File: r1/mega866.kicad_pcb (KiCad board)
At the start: 2 copper layers, 2 parts, among them J1 5650908-5, J2 5650908-5

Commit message: cleaner drc / fix errors
Signed-off-by: John McMaster <johndmcmaster@gmail.com>
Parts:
- added D1: LED, LED_SMD:LED_0603_1608Metric, F.Cu at (-44.7, 45.7)
- added D2: LED, LED_SMD:LED_0603_1608Metric, F.Cu at (-48.8, 45.7)
- added J5: Conn_01x02_Male, Connector_PinHeader_2.54mm:PinHeader_1x02_P2.54mm_Vertical, F.Cu at (-91.9, 100.4)
- added J8: Conn_01x02_Male, Connector_PinHeader_2.54mm:PinHeader_1x02_P2.54mm_Vertical, F.Cu at (-67.8, 46.8)
- added Q1: BSS84, Package_TO_SOT_SMD:SOT-23, F.Cu at (-63.0, 46.6)
- added Q2: 2N7002, Package_TO_SOT_SMD:SOT-23, F.Cu at (-53.2, 46.6)
- added Q3: 2N7002, Package_TO_SOT_SMD:SOT-23, F.Cu at (-58.1, 46.6)
- added R1: R, Resistor_SMD:R_0603_1608Metric, F.Cu at (-47.4, 48.3)
- added R10: NOLOAD, Resistor_SMD:R_0603_1608Metric, F.Cu at (-43.4, 53.2)
- added R11: 4.7k, Resistor_SMD:R_0603_1608Metric, F.Cu at (-51.4, 50.1)
- added R12: 0, Resistor_SMD:R_0603_1608Metric, F.Cu at (-60.1, 53.2)
- added R13: 0, Resistor_SMD:R_0603_1608Metric, F.Cu at (-68.1, 55.7)
- added R14: 0, Resistor_SMD:R_0603_1608Metric, F.Cu at (-39.4, 50.7)
- added R15: 100k, Resistor_SMD:R_0603_1608Metric, F.Cu at (-64.1, 53.2)
- added R17: 4.7K, Resistor_SMD:R_0603_1608Metric, F.Cu at (-59.5, 50.1)
- added R18: 0, Resistor_SMD:R_0603_1608Metric, F.Cu at (-56.1, 55.1)
- added R19: 0, Resistor_SMD:R_0603_1608Metric, F.Cu at (-52.1, 52.6)
- added R2: R, Resistor_SMD:R_0603_1608Metric, F.Cu at (-47.4, 50.8)
- added R20: 0, Resistor_SMD:R_0603_1608Metric, F.Cu at (-52.1, 55.1)
- added R21: 0, Resistor_SMD:R_0603_1608Metric, F.Cu at (-36.7, 48.2)
- added R22: 0, Resistor_SMD:R_0603_1608Metric, F.Cu at (-40.7, 45.7)
- added R23: 0, Resistor_SMD:R_0603_1608Metric, F.Cu at (-55.4, 50.1)
- added R3: 47k, Resistor_SMD:R_0603_1608Metric, F.Cu at (-63.5, 50.7)
- added R4: 4.7k, Resistor_SMD:R_0603_1608Metric, F.Cu at (-36.7, 45.7)
- added R5: 4.7k, Resistor_SMD:R_0603_1608Metric, F.Cu at (-32.7, 45.7)
- added R6: 47k, Resistor_SMD:R_0603_1608Metric, F.Cu at (-39.4, 53.2)
- added R7: NOLOAD, Resistor_SMD:R_0603_1608Metric, F.Cu at (-40.7, 48.2)
- added R8: NOLOAD, Resistor_SMD:R_0603_1608Metric, F.Cu at (-56.1, 52.6)
- added R9: NOLOAD, Resistor_SMD:R_0603_1608Metric, F.Cu at (-43.4, 50.7)
- added U1: Pico, mega866:RPi_Pico_SMD_TH, F.Cu at (-82.2, 71.0)

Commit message: WIP
Signed-off-by: John McMaster <johndmcmaster@gmail.com>
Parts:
- added J10: Conn_01x06_Male, Connector_PinHeader_2.54mm:PinHeader_1x06_P2.54mm_Vertical, B.Cu at (171.4, 149.7)
- added J3: tl866_dip40, mega866:tl866, F.Cu at (64.6, 4.91)
- added J4: Conn_01x06_Male, Connector_PinHeader_2.54mm:PinHeader_1x06_P2.54mm_Vertical, B.Cu at (116.8, 30.3)
- added J5: tl866_dip40, mega866:tl866, F.Cu at (211.9, 53.2)
- added J6: Conn_01x06_Male, Connector_PinHeader_2.54mm:PinHeader_1x06_P2.54mm_Vertical, B.Cu at (171.4, 78.6)
- added J7: tl866_dip40, mega866:tl866, F.Cu at (64.6, 126.8)
- added J8: Conn_01x06_Male, Connector_PinHeader_2.54mm:PinHeader_1x06_P2.54mm_Vertical, B.Cu at (116.8, 101.4)
- added J9: tl866_dip40, mega866:tl866, F.Cu at (211.9, 175.1)
- D1, D2, Q1, Q2, Q3, R1, R10, R11, R12, R13, R14, R15, R17, R18, R19, R2, R20, R21, R22, R23, R3, R4, R5, R6, R7, R8, R9, U1: moved to B.Cu
- J1: renamed from J2; value 5650908-5 -> ZSM1-SM1; footprint 5650908-5:TE_5650908-5 -> mega866:5650470-5
- J11: renamed from J5; moved to B.Cu
- J12: renamed from J8; moved to B.Cu
- J2: renamed from J1; value 5650908-5 -> ZSM1-SM2; footprint 5650908-5:TE_5650908-5 -> mega866:5650470-5
- moved R15 235.8 mm to (151.1, -43.2), turned to 180 degrees
- moved R12 228.5 mm to (147.1, -43.2), turned to 180 degrees
- moved R17 227.4 mm to (146.5, -46.3), turned to 180 degrees
- moved R2 221.9 mm to (137.2, 174.0), turned to 180 degrees
- moved D2 221.7 mm to (132.1, 174.0), turned to 180 degrees
- moved U1 220.3 mm to (137.3, 90.2)
- moved R11 213.0 mm to (138.5, -46.3), turned to 180 degrees
- moved R13 209.2 mm to (129.5, -12.7), turned to 180 degrees
- moved D1 207.9 mm to (118.9, 174.0), turned to 180 degrees
- moved J11 207.3 mm to (114.3, 121.9)
- moved R1 204.8 mm to (114.3, 174.0), turned to 180 degrees
- moved J12 201.2 mm to (133.3, 50.8), turned to -90 degrees
- moved Q3 200.7 mm to (125.7, 127.0)
- moved R3 196.7 mm to (119.4, 123.2), turned to 90 degrees
- moved Q1 194.6 mm to (113.0, 129.5), turned to 180 degrees
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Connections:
- J1 pad A1: (no net) -> GND
- J1 pad A10: (no net) -> G037
- J1 pad A11: (no net) -> G035
- J1 pad A12: (no net) -> G033
- J1 pad A13: (no net) -> G031
- J1 pad A14: (no net) -> G029
- J1 pad A15: (no net) -> G027
- J1 pad A16: (no net) -> G025
- J1 pad A17: (no net) -> G023
- J1 pad A18: (no net) -> G021
- J1 pad A19: (no net) -> G019
- J1 pad A2: (no net) -> Net-(J1-PadA2)
- J1 pad A20: (no net) -> G017
- J1 pad A21: (no net) -> G015
- J1 pad A22: (no net) -> G013
- J1 pad A23: (no net) -> G011
- J1 pad A24: (no net) -> G009
- J1 pad A25: (no net) -> G007
- J1 pad A26: (no net) -> G005
- J1 pad A27: (no net) -> G003
- J1 pad A28: (no net) -> G001
- J1 pad A29: (no net) -> GND
- J1 pad A3: (no net) -> Net-(J1-PadA2)
- J1 pad A30: (no net) -> P2R
- J1 pad A31: (no net) -> VCC
- J1 pad A32: (no net) -> GND
- J1 pad A4: (no net) -> GND
- J1 pad A5: (no net) -> G047
- J1 pad A6: (no net) -> G045
- J1 pad A7: (no net) -> G043
- J1 pad A8: (no net) -> G041
- J1 pad A9: (no net) -> G039
- J1 pad B1: (no net) -> G159
- J1 pad B10: (no net) -> G141
- J1 pad B11: (no net) -> G139
- J1 pad B12: (no net) -> G137
- J1 pad B13: (no net) -> G135
- J1 pad B14: (no net) -> G133
- J1 pad B15: (no net) -> G131
- J1 pad B16: (no net) -> G129
- J1 pad B17: (no net) -> G127
- J1 pad B18: (no net) -> G125
- J1 pad B19: (no net) -> G123
- J1 pad B2: (no net) -> G157
- J1 pad B20: (no net) -> G121
- J1 pad B21: (no net) -> G119
- J1 pad B22: (no net) -> G117
- J1 pad B23: (no net) -> G115
- J1 pad B24: (no net) -> G113
- J1 pad B25: (no net) -> G111
- J1 pad B26: (no net) -> G109
- J1 pad B27: (no net) -> G107
- J1 pad B28: (no net) -> G105
- J1 pad B29: (no net) -> G103
- J1 pad B3: (no net) -> G155
- J1 pad B30: (no net) -> G101
- J1 pad B31: (no net) -> G099
- J1 pad B32: (no net) -> G097
- J1 pad B4: (no net) -> G153
- J1 pad B5: (no net) -> G151
- J1 pad B6: (no net) -> G149
- J1 pad B7: (no net) -> G147
- J1 pad B8: (no net) -> G145
- J1 pad B9: (no net) -> G143
- J1 pad C1: (no net) -> BPM_SR_CLK
- J1 pad C10: (no net) -> G087
- J1 pad C11: (no net) -> GND
- J1 pad C12: (no net) -> G085
- J1 pad C13: (no net) -> G083
- J1 pad C14: (no net) -> G081
- J1 pad C15: (no net) -> G079
- J1 pad C16: (no net) -> G077
- J1 pad C17: (no net) -> GND
- J1 pad C18: (no net) -> G075
- J1 pad C19: (no net) -> G073
- J1 pad C2: (no net) -> BPM_SR_D
- J1 pad C20: (no net) -> G071
- J1 pad C21: (no net) -> G069
- J1 pad C22: (no net) -> G067
- J1 pad C23: (no net) -> GND
- J1 pad C24: (no net) -> G065
- J1 pad C25: (no net) -> G063
- J1 pad C26: (no net) -> G061
- J1 pad C27: (no net) -> G059
- J1 pad C28: (no net) -> G057
- J1 pad C29: (no net) -> G055
- J1 pad C3: (no net) -> Net-(J1-PadC3)
- J1 pad C30: (no net) -> G053
- J1 pad C31: (no net) -> G051
- J1 pad C32: (no net) -> G049
- J1 pad C4: (no net) -> Net-(J1-PadC4)
- J1 pad C5: (no net) -> SM1_C5
- J1 pad C6: (no net) -> G095
- J1 pad C7: (no net) -> G093
- J1 pad C8: (no net) -> G091
- J1 pad C9: (no net) -> G089
- J11 pad 1: P2R -> Net-(J11-Pad1)
- J11 pad 2: COIL_GPIO -> VCC
- J12 pad 1: Net-(J8-Pad1) -> P2R
- J12 pad 2: VCC -> COIL_GPIO
- J2 pad A1: (no net) -> EEPROM_DO
- J2 pad A10: (no net) -> G088
- J2 pad A11: (no net) -> GND
- J2 pad A12: (no net) -> G086
- J2 pad A13: (no net) -> G084
- J2 pad A14: (no net) -> G082
- J2 pad A15: (no net) -> G080
- J2 pad A16: (no net) -> G078
- J2 pad A17: (no net) -> GND
- J2 pad A18: (no net) -> G076
- J2 pad A19: (no net) -> G074
- J2 pad A2: (no net) -> EEPROM_DI
- J2 pad A20: (no net) -> G072
- J2 pad A21: (no net) -> G070
- J2 pad A22: (no net) -> G068
- J2 pad A23: (no net) -> GND
- J2 pad A24: (no net) -> G066
- J2 pad A25: (no net) -> G064
- J2 pad A26: (no net) -> G062
- J2 pad A27: (no net) -> G060
- J2 pad A28: (no net) -> G058
- J2 pad A29: (no net) -> G056
- J2 pad A3: (no net) -> EEPROM_CLK
- J2 pad A30: (no net) -> G054
- J2 pad A31: (no net) -> G052
- J2 pad A32: (no net) -> G050
- J2 pad A4: (no net) -> EEPROM_CS
- J2 pad A5: (no net) -> SM2_A5
- J2 pad A6: (no net) -> G096
- J2 pad A7: (no net) -> G094
- J2 pad A8: (no net) -> G092
- J2 pad A9: (no net) -> G090
- J2 pad B1: (no net) -> G160
- J2 pad B10: (no net) -> G142
- J2 pad B11: (no net) -> G140
- J2 pad B12: (no net) -> G138
- J2 pad B13: (no net) -> G136
- J2 pad B14: (no net) -> G134
- J2 pad B15: (no net) -> G132
- J2 pad B16: (no net) -> G130
- J2 pad B17: (no net) -> G128
- J2 pad B18: (no net) -> G126
- J2 pad B19: (no net) -> G124
- J2 pad B2: (no net) -> G158
- J2 pad B20: (no net) -> G122
- J2 pad B21: (no net) -> G120
- J2 pad B22: (no net) -> G118
- J2 pad B23: (no net) -> G116
- J2 pad B24: (no net) -> G114
- J2 pad B25: (no net) -> G112
- J2 pad B26: (no net) -> G110
- J2 pad B27: (no net) -> G108
- J2 pad B28: (no net) -> G106
- J2 pad B29: (no net) -> G104
- J2 pad B3: (no net) -> G156
- J2 pad B30: (no net) -> G102
- J2 pad B31: (no net) -> G100
- J2 pad B32: (no net) -> G098
- J2 pad B4: (no net) -> G154
- J2 pad B5: (no net) -> G152
- J2 pad B6: (no net) -> G150
- J2 pad B7: (no net) -> G148
- J2 pad B8: (no net) -> G146
- J2 pad B9: (no net) -> G144
- J2 pad C1: (no net) -> GND
- J2 pad C10: (no net) -> G038
- J2 pad C11: (no net) -> G036
- J2 pad C12: (no net) -> G034
- J2 pad C13: (no net) -> G032
- J2 pad C14: (no net) -> G030
- J2 pad C15: (no net) -> G028
- J2 pad C16: (no net) -> G026
- J2 pad C17: (no net) -> G024
- J2 pad C18: (no net) -> G022
- J2 pad C19: (no net) -> G020
- J2 pad C2: (no net) -> SM_DET
- J2 pad C20: (no net) -> G018
- J2 pad C21: (no net) -> G016
- J2 pad C22: (no net) -> G014
- J2 pad C23: (no net) -> G012
- J2 pad C24: (no net) -> G010
- J2 pad C25: (no net) -> G008
- J2 pad C26: (no net) -> G006
- J2 pad C27: (no net) -> G004
- J2 pad C28: (no net) -> G002
- J2 pad C29: (no net) -> GND
- J2 pad C3: (no net) -> SM2_C3
- J2 pad C30: (no net) -> Net-(J2-PadC30)
- J2 pad C31: (no net) -> unconnected-(J2-PadC31)
- J2 pad C32: (no net) -> GND
- J2 pad C4: (no net) -> COILP
- J2 pad C5: (no net) -> G048
- J2 pad C6: (no net) -> G046
- J2 pad C7: (no net) -> G044
- J2 pad C8: (no net) -> G042
- J2 pad C9: (no net) -> G040
- Q1 pad 1: Net-(J8-Pad1) -> Net-(Q1-Pad1)
- Q1 pad 2: Net-(J8-Pad1) -> Net-(J11-Pad1)
- Q1 pad 3: Net-(J8-Pad1) -> COILP
- Q2 pad 3: Net-(Q1-Pad4) -> Net-(Q1-Pad1)
- R11 pad 1: EEPROM CS -> EEPROM_CS
- R3 pad 1: Net-(Q1-Pad4) -> Net-(Q1-Pad1)
- R3 pad 2: Net-(J8-Pad1) -> Net-(J11-Pad1)
- U1 pad 1: EEPROM DO -> EEPROM_DO
- U1 pad 2: EEPROM CS -> EEPROM_CS
- U1 pad 4: EEPROM CLK -> EEPROM_CLK
- U1 pad 5: EEPROM DI -> EEPROM_DI
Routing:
- net G048: track 0.00 -> 103.5 mm
- net G044: track 0.00 -> 101.0 mm
- net G040: track 0.00 -> 98.4 mm
- net G036: track 0.00 -> 95.9 mm
- net G032: track 0.00 -> 93.4 mm
- net G046: track 0.00 -> 91.2 mm
- net G028: track 0.00 -> 90.8 mm
- net G042: track 0.00 -> 88.6 mm
- net G024: track 0.00 -> 88.3 mm
- net G038: track 0.00 -> 86.1 mm
- net G020: track 0.00 -> 85.6 mm
- net G034: track 0.00 -> 83.8 mm
- net G016: track 0.00 -> 83.2 mm
- net G030: track 0.00 -> 81.0 mm
- net G012: track 0.00 -> 80.5 mm
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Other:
- board outline added: 10 x 4 mm

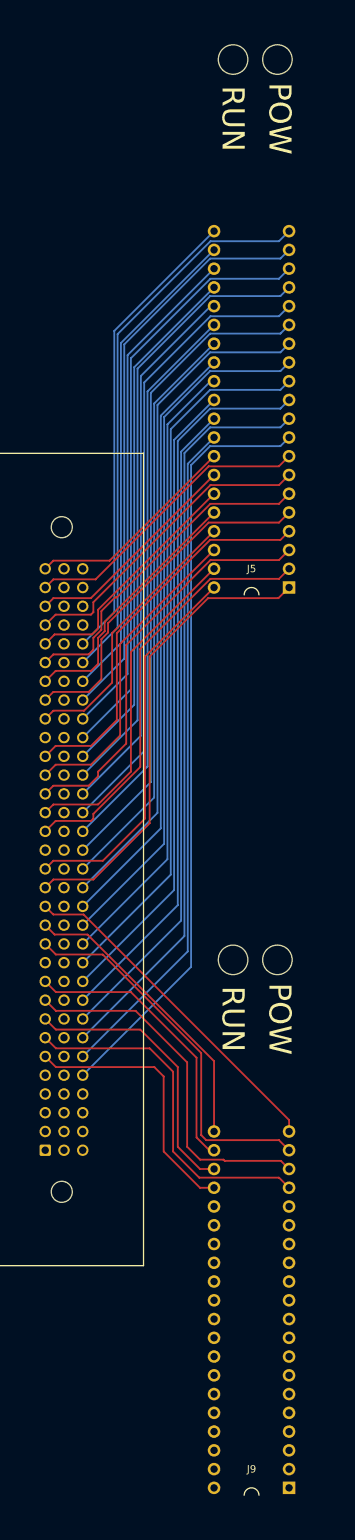
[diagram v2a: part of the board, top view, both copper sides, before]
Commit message: reassign pins for easier routing
Signed-off-by: John McMaster <johndmcmaster@gmail.com>
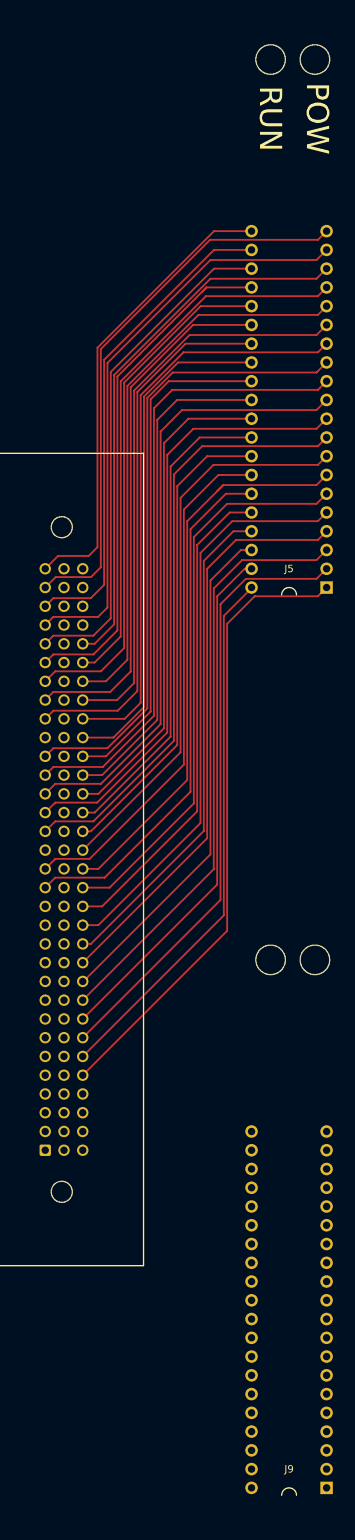
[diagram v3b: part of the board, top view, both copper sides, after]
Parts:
- moved J5 5.08 mm to (217.0, 53.2)
- moved J9 5.08 mm to (217.0, 175.1)
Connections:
- J5 pad 1: G080 -> G048
- J5 pad 10: G044 -> G074
- J5 pad 11: G040 -> G072
- J5 pad 12: G036 -> G070
- J5 pad 13: G032 -> G068
- J5 pad 14: G028 -> G010
- J5 pad 15: G024 -> G008
- J5 pad 16: G020 -> G006
- J5 pad 17: G016 -> G004
- J5 pad 18: G012 -> G002
- J5 pad 19: G008 -> G056
- J5 pad 2: G076 -> G044
- J5 pad 20: G004 -> G052
- J5 pad 21: G002 -> G050
- J5 pad 22: G006 -> G054
- J5 pad 23: G010 -> G058
- J5 pad 24: G014 -> G060
- J5 pad 25: G018 -> G062
- J5 pad 26: G022 -> G064
- J5 pad 27: G026 -> G066
- J5 pad 28: G030 -> G012
- J5 pad 29: G034 -> G014
- J5 pad 3: G072 -> G040
- J5 pad 30: G038 -> G016
- J5 pad 31: G042 -> G018
- J5 pad 32: G046 -> G020
- J5 pad 33: G050 -> G022
- J5 pad 34: G054 -> G078
- J5 pad 35: G058 -> G080
- J5 pad 36: G062 -> G030
- J5 pad 37: G066 -> G034
- J5 pad 38: G070 -> G038
- J5 pad 39: G074 -> G042
- J5 pad 4: G068 -> G036
- J5 pad 40: G078 -> G046
- J5 pad 5: G064 -> G032
- J5 pad 6: G060 -> G028
- J5 pad 7: G056 -> G026
- J5 pad 8: G052 -> G024
- J5 pad 9: G048 -> G076
- J9 pad 10: G122 -> G084
- J9 pad 11: G118 -> G082
- J9 pad 12: G114 -> G130
- J9 pad 13: G110 -> G126
- J9 pad 14: G106 -> G122
- J9 pad 15: G102 -> G118
- J9 pad 16: G098 -> G114
- J9 pad 17: G094 -> G110
- J9 pad 18: G090 -> G106
- J9 pad 19: G086 -> G102
- J9 pad 20: G082 -> G098
- J9 pad 21: G084 -> G100
- J9 pad 22: G088 -> G104
- J9 pad 23: G092 -> G108
- J9 pad 24: G096 -> G112
- J9 pad 25: G100 -> G116
- J9 pad 26: G104 -> G120
- J9 pad 27: G108 -> G124
- J9 pad 28: G112 -> G128
- J9 pad 29: G116 -> G132
- J9 pad 30: G120 -> G134
- J9 pad 31: G124 -> G136
- J9 pad 32: G128 -> G138
- J9 pad 33: G132 -> G088
- J9 pad 34: G136 -> G090
- J9 pad 35: G140 -> G092
- J9 pad 36: G144 -> G094
- J9 pad 37: G148 -> G096
- J9 pad 4: G146 -> G148
- J9 pad 5: G142 -> G146
- J9 pad 6: G138 -> G144
- J9 pad 7: G134 -> G142
- J9 pad 8: G130 -> G140
- J9 pad 9: G126 -> G086
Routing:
- net G086: track 51.1 -> 0.00 mm
- net G090: track 49.2 -> 0.00 mm
- net G094: track 47.8 -> 0.00 mm
- net G082: track 46.6 -> 0.00 mm
- net G070: track 42.8 -> 84.6 mm
- net G084: track 40.0 -> 0.00 mm
- net G088: track 38.7 -> 0.00 mm
- net G092: track 37.6 -> 0.00 mm
- net G056: track 42.2 -> 78.5 mm
- net G074: track 46.0 -> 82.2 mm
- net G096: track 36.2 -> 0.00 mm
- net G058: track 32.8 -> 68.5 mm
- net G054: track 30.2 -> 65.8 mm
- net G066: track 37.3 -> 72.7 mm
- net G052: track 40.4 -> 75.4 mm
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
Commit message: release candidate
Signed-off-by: John McMaster <johndmcmaster@gmail.com>
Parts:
- added R16: 0, Resistor_SMD:R_0603_1608Metric, B.Cu at (100.0, 133.8)
- added R24: 0, Resistor_SMD:R_0603_1608Metric, B.Cu at (100.0, 130.8)
- D1, D2: moved to F.Cu
- moved R15 174.5 mm to (176.5, 129.5), turned to 90 degrees
- moved R12 170.3 mm to (170.2, 125.5)
- moved R11 167.3 mm to (151.5, 120.5), turned to 90 degrees
- moved R14 164.8 mm to (98.7, 116.8), turned to 0 degrees
- moved R13 140.1 mm to (176.5, 119.2)
- moved R21 134.7 mm to (120.7, 86.4), turned to 0 degrees
- moved R9 117.0 mm to (120.7, 76.3), turned to 0 degrees
- moved R17 106.5 mm to (177.0, 55.8)
- moved D1 44.5 mm to (134.2, 132.2), turned to 90 degrees
- moved D2 42.5 mm to (140.2, 132.2), turned to 90 degrees
- moved R1 40.1 mm to (134.2, 139.2), turned to -90 degrees
- moved R2 34.9 mm to (140.2, 139.2), turned to -90 degrees
- moved J12 32.4 mm to (101.5, 57.0)
- moved R5 29.1 mm to (100.2, 120.8), turned to 90 degrees
- moved R8 28.3 mm to (97.8, 125.2), turned to 90 degrees
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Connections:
- J1 pad C1: BPM_SR_CLK -> Net-(J1-PadC1)
- J1 pad C2: BPM_SR_D -> Net-(J1-PadC2)
- J3 pad 1: G001 -> G051
- J3 pad 10: G037 -> G071
- J3 pad 11: G041 -> G073
- J3 pad 12: G045 -> G075
- J3 pad 13: G049 -> G023
- J3 pad 14: G053 -> G025
- J3 pad 15: G057 -> G027
- J3 pad 16: G061 -> G031
- J3 pad 17: G065 -> G035
- J3 pad 18: G069 -> G039
- J3 pad 19: G073 -> G043
- J3 pad 2: G005 -> G055
- J3 pad 20: G077 -> G047
- J3 pad 21: G079 -> G045
- J3 pad 22: G075 -> G041
- J3 pad 23: G071 -> G037
- J3 pad 24: G067 -> G033
- J3 pad 25: G063 -> G029
- J3 pad 26: G059 -> G079
- J3 pad 27: G055 -> G077
- J3 pad 28: G051 -> G021
- J3 pad 29: G047 -> G019
- J3 pad 3: G009 -> G001
- J3 pad 30: G043 -> G017
- J3 pad 31: G039 -> G015
- J3 pad 32: G035 -> G013
- J3 pad 33: G031 -> G011
- J3 pad 34: G027 -> G065
- J3 pad 35: G023 -> G063
- J3 pad 36: G019 -> G061
- J3 pad 37: G015 -> G059
- J3 pad 38: G011 -> G057
- J3 pad 39: G007 -> G053
- J3 pad 4: G013 -> G003
- J3 pad 40: G003 -> G049
- J3 pad 5: G017 -> G005
- J3 pad 6: G021 -> G007
- J3 pad 7: G025 -> G009
- J3 pad 8: G029 -> G067
- J3 pad 9: G033 -> G069
- J7 pad 1: G081 -> G097
- J7 pad 10: G117 -> G133
- J7 pad 11: G121 -> G135
- J7 pad 12: G125 -> G137
- J7 pad 13: G129 -> G139
- J7 pad 14: G133 -> G087
- J7 pad 15: G137 -> G089
- J7 pad 16: G141 -> G091
- J7 pad 17: G145 -> G093
- J7 pad 18: G149 -> G095
- J7 pad 2: G085 -> G101
- J7 pad 24: G147 -> G149
- J7 pad 25: G143 -> G147
- J7 pad 26: G139 -> G145
- J7 pad 27: G135 -> G143
- J7 pad 28: G131 -> G141
- J7 pad 29: G127 -> G085
- J7 pad 3: G089 -> G105
- J7 pad 30: G123 -> G083
- J7 pad 31: G119 -> G081
- J7 pad 32: G115 -> G131
- J7 pad 33: G111 -> G127
- J7 pad 34: G107 -> G123
- J7 pad 35: G103 -> G119
- J7 pad 36: G099 -> G115
- J7 pad 37: G095 -> G111
- J7 pad 38: G091 -> G107
- J7 pad 39: G087 -> G103
- J7 pad 4: G093 -> G109
- J7 pad 40: G083 -> G099
- J7 pad 5: G097 -> G113
- J7 pad 6: G101 -> G117
- J7 pad 7: G105 -> G121
- J7 pad 8: G109 -> G125
- J7 pad 9: G113 -> G129
- J9 pad 10: G084 -> G136
- J9 pad 11: G082 -> G134
- J9 pad 3: G150 -> G096
- J9 pad 30: G134 -> G082
- J9 pad 31: G136 -> G084
- J9 pad 32: G138 -> G086
- J9 pad 33: G088 -> G142
- J9 pad 34: G090 -> G144
- J9 pad 35: G092 -> G146
- J9 pad 36: G094 -> G148
- J9 pad 37: G096 -> G150
- J9 pad 4: G148 -> G094
- J9 pad 5: G146 -> G092
- J9 pad 6: G144 -> G090
- J9 pad 7: G142 -> G088
- J9 pad 9: G086 -> G138
- R18 pad 1: G033 -> G045
- R18 pad 2: G033_GPIO -> G045_GPIO
- R19 pad 1: G037 -> G043
- R19 pad 2: G037_GPIO -> G043_GPIO
- R20 pad 1: G039 -> G041
- R20 pad 2: G039_GPIO -> G041_GPIO
- R21 pad 1: G041 -> G039
- R21 pad 2: G041_GPIO -> G039_GPIO
- R22 pad 1: G043 -> G037
- R22 pad 2: G043_GPIO -> G037_GPIO
- R23 pad 1: G045 -> G033
- R23 pad 2: G045_GPIO -> G033_GPIO
- U1 pad 10: G037_GPIO -> G043_GPIO
- U1 pad 11: G039_GPIO -> G041_GPIO
- U1 pad 12: G041_GPIO -> G039_GPIO
- U1 pad 14: G043_GPIO -> G037_GPIO
- U1 pad 15: G045_GPIO -> G033_GPIO
- U1 pad 9: G033_GPIO -> G045_GPIO
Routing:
- net GND: track 11.1 -> 595.0 mm, vias 0 -> 7
- net VCC: track 0.00 -> 177.7 mm, vias 0 -> 2
- net G043: track 0.00 -> 176.2 mm, vias 0 -> 3
- net COILP: track 0.00 -> 125.1 mm, vias 0 -> 1
- net G039: track 0.00 -> 122.3 mm
- net G045: track 0.00 -> 116.1 mm, vias 0 -> 1
- net G041: track 0.00 -> 112.7 mm
- net G037: track 0.00 -> 112.2 mm
- net G033: track 0.00 -> 109.2 mm
- net G098: track 0.00 -> 98.2 mm
- net G097: track 0.00 -> 98.2 mm
- net G102: track 0.00 -> 95.8 mm
- net G101: track 0.00 -> 95.8 mm
- net G105: track 0.00 -> 93.9 mm
- net G106: track 0.00 -> 93.9 mm
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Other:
- board size 10 x 4 mm -> 170.5 x 172.7 mm

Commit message: tweaks
Signed-off-by: John McMaster <johndmcmaster@gmail.com>
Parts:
- moved D1 25.2 mm to (133.7, 157.5), turned to -90 degrees
- moved D2 25.2 mm to (139.7, 157.5), turned to -90 degrees
- moved R1 12.7 mm to (133.7, 151.9), turned to 90 degrees
- moved R2 12.7 mm to (139.7, 151.9), turned to 90 degrees
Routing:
- net LED1: track 80.0 -> 109.2 mm
- net LED2: track 79.5 -> 107.1 mm
- net GND: track 595.0 -> 613.9 mm
- net COILP: track 125.1 -> 142.0 mm
- net Net-(D2-Pad1): track 5.39 -> 3.92 mm
- net G026: track 76.8 -> 75.6 mm
- net G025: track 76.8 -> 75.6 mm
- net Net-(D1-Pad1): track 5.39 -> 4.21 mm
- net G059: track 70.0 -> 69.1 mm
- net G060: track 70.0 -> 69.1 mm
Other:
- board text added: "MEGA866 (C) 2022 JOHN MCMASTER https://github.com/JohnDMcMaster/mega866-cad/"

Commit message: releasing
Signed-off-by: John McMaster <johndmcmaster@gmail.com>
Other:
- board text added: "AUTOBOTS IS BEST BOTS"
- board text added: "EARTH"
- board text added: "FIRE"
- board text added: "HEART"
- board text added: "NEED MOAR ALLSPARK"
- board text added: "WATER"
- board text added: "WIND"
